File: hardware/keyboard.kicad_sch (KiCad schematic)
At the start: 41 parts, among them SW1 SW_Push, SW10 SW_Push, SW11 SW_Push, SW12 SW_Push, SW13 SW_Push, SW14 SW_Push, SW15 SW_Push, SW16 SW_Push, SW17 SW_Push, SW18 SW_Push, SW19 SW_Push, SW2 SW_Push, SW20 SW_Push, SW21 SW_Push, SW22 SW_Push, SW23 SW_Push, SW24 SW_Push, SW25 SW_Push, SW26 SW_Push, SW27 SW_Push, SW28 SW_Push, SW29 SW_Push, SW3 SW_Push, SW30 SW_Push, SW31 SW_Push, SW32 SW_Push, SW33 SW_Push, SW34 SW_Push, SW35 SW_Push, SW36 SW_Push, SW37 SW_Push, SW38 SW_Push, SW39 SW_Push, SW4 SW_Push, SW40 SW_Push, SW5 SW_Push, SW6 SW_Push, SW7 SW_Push, SW8 SW_Push, SW9 SW_Push, U2 74HC138

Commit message: keyboard schematic
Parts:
- added R23, R24, R25, R26, R27, R28, R29, R30: 22, symbol Device:R
- added SW42, SW43, SW44, SW45, SW46, SW47, SW48, SW49, SW50, SW51, SW52, SW53, SW54, SW55, SW56, SW57: SW_Push, Button_Switch_SMD:SW_Push_1P1T_NO_6x6mm_H9.5mm, symbol Switch:SW_Push
- U2: LCSC (none) -> C2906780
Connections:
- net at SW34.1: now also SW28.1, SW29.1, SW30.1, SW31.1, SW32.1, SW35.1, R26.2
- net KB_COL5: now reaches SW34.2
- net KB_COL5: now also SW10.2, SW18.2, SW26.2, SW3.2, SW42.2, SW49.2, SW56.2
- net at SW14.1: now also SW12.1, SW13.1, SW15.1, SW16.1, SW18.1, SW19.1, R28.2
- net KB_COL2: now reaches SW14.2
- net KB_COL2: now also SW17.2, SW22.2, SW30.2, SW38.2, SW6.2, SW46.2, SW53.2
- net at SW33.1: now also SW1.1, SW17.1, SW25.1, SW3.1, SW4.1, SW9.1, R30.2
- net KB_COL4: now reaches SW33.2
- net KB_COL4: now also SW16.2, SW24.2, SW32.2, SW40.2, SW8.2, SW48.2, SW55.2
- net at SW6.1: now also SW10.1, SW11.1, SW2.1, SW5.1, SW7.1, SW8.1, R29.2
- net KB_COL3: now reaches SW31.2
- net KB_COL3: now also SW15.2, SW23.2, SW25.2, SW39.2, SW7.2, SW47.2, SW54.2
- net KB_COL1: now reaches SW9.2
- net KB_COL1: now also SW13.2, SW21.2, SW29.2, SW37.2, SW5.2, SW45.2, SW52.2
- net KB_COL6: now reaches SW11.2
- net KB_COL6: now also SW19.2, SW27.2, SW35.2, SW4.2, SW43.2, SW50.2, SW57.2
- net at SW39.1: now also SW36.1, SW37.1, SW38.1, SW40.1, R25.2, SW42.1, SW43.1
- net KB_COL0: now reaches SW1.2
- net KB_COL0: now also SW12.2, SW2.2, SW20.2, SW28.2, SW36.2, SW44.2, SW51.2
- net at SW23.1: now also SW20.1, SW21.1, SW22.1, SW24.1, SW26.1, SW27.1, R27.2
- net KB_ROW0: now reaches U2.1 (A0)
- net at U2.10 (~{Y5}): now also R28.1
- net at U2.11 (~{Y4}): now also R27.1
- net at U2.12 (~{Y3}): now also R26.1
- net at U2.13 (~{Y2}): now also R25.1
- net at U2.14 (~{Y1}): now also R24.1
- net at U2.15 (~{Y0}): now also R23.1
- net +3.3V: now reaches U2.16 (VCC)
- net +3.3V: now also U2.6 (E2)
- net KB_ROW1: now reaches U2.2 (A1)
- net KB_ROW2: now reaches U2.3 (A2)
- net GND: now reaches U2.4 (~{E0})
- net GND: now also U2.5 (~{E1}), U2.8 (GND)
- net at U2.7 (~{Y7}): now also R30.1
- net at U2.9 (~{Y6}): now also R29.1
- new net: R24.2, SW44.1, SW45.1, SW46.1, SW47.1, SW48.1, SW49.1, SW50.1
- new net: R23.2, SW51.1, SW52.1, SW53.1, SW54.1, SW55.1, SW56.1, SW57.1
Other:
- moved on the sheet: SW1, SW17, SW25, SW33, SW9, U2

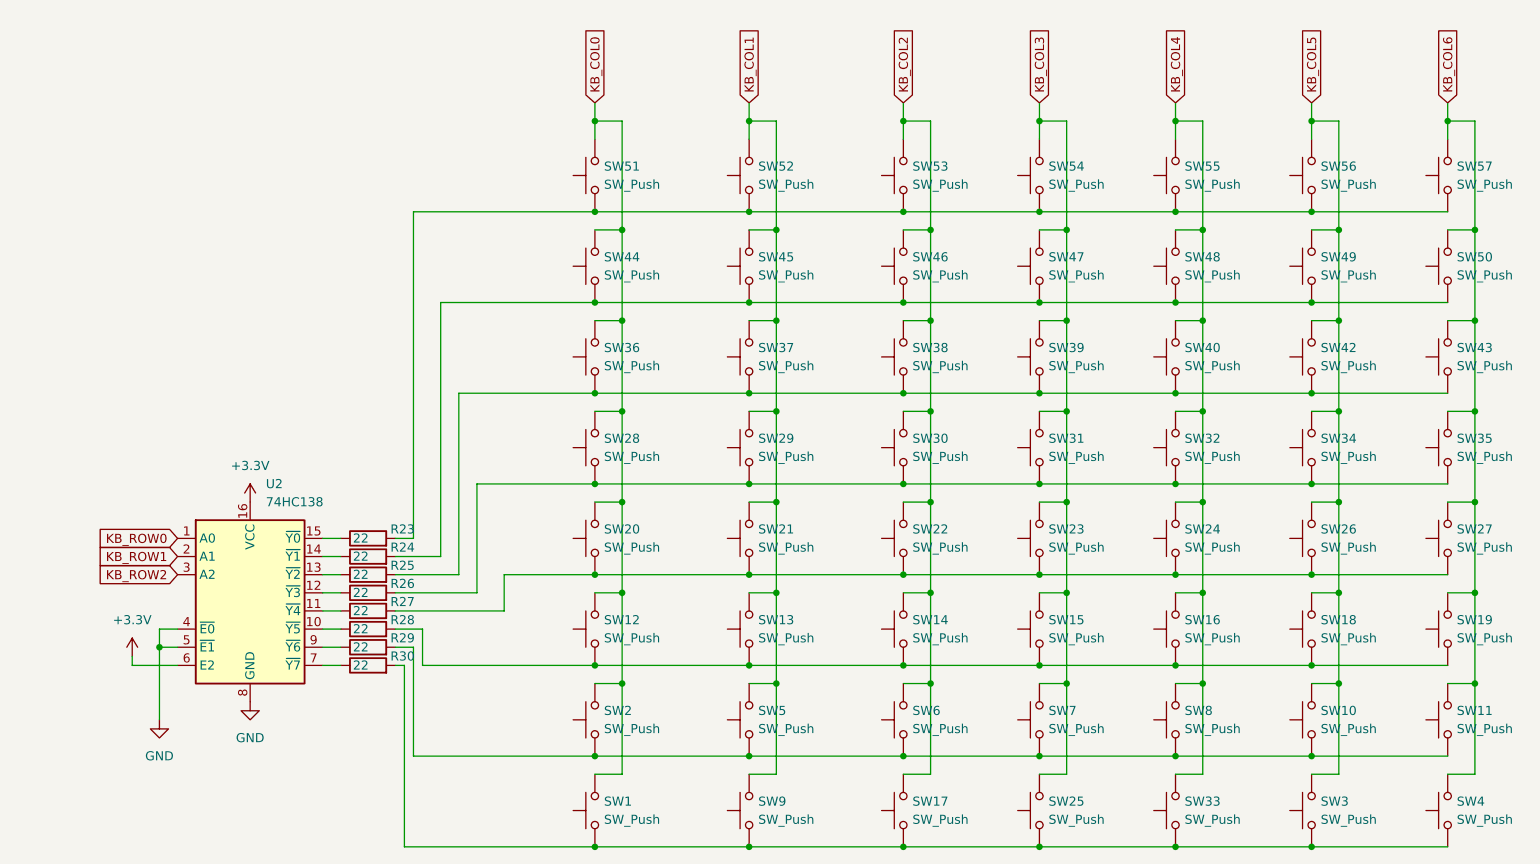
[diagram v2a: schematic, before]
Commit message: update usb port, esd, lcsc
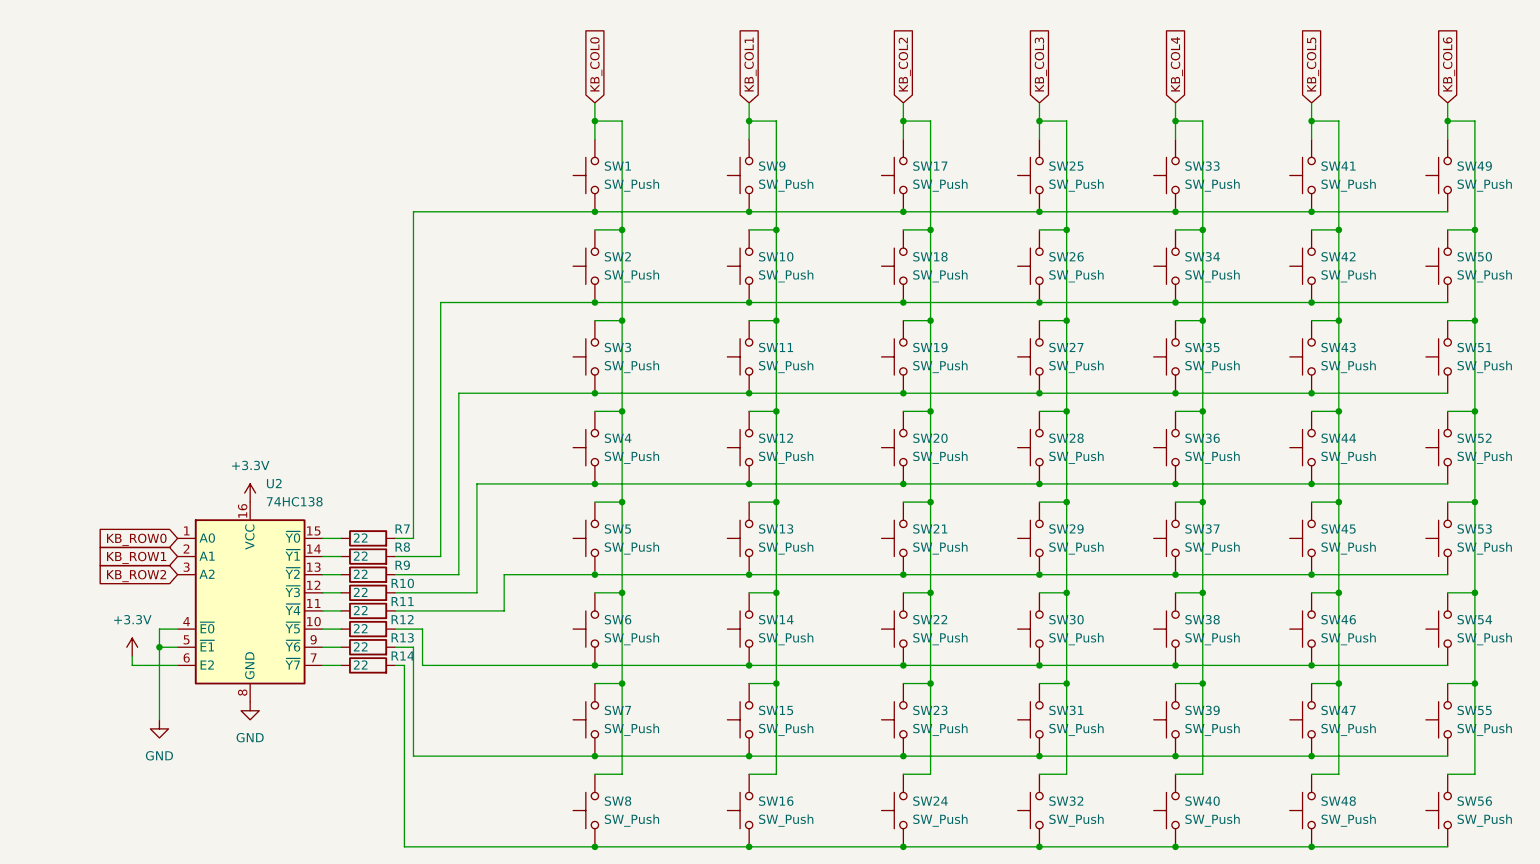
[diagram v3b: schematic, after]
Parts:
- renumbered R26 to R10, R27 to R11, R28 to R12, R29 to R13, R30 to R14, R23 to R7, R24 to R8, R25 to R9, SW51 to SW1, SW45 to SW10, SW37 to SW11, SW29 to SW12, SW21 to SW13, SW13 to SW14, SW5 to SW15, SW9 to SW16, SW53 to SW17, SW46 to SW18, SW38 to SW19, SW44 to SW2, SW30 to SW20, SW22 to SW21, SW14 to SW22, SW6 to SW23, SW17 to SW24, SW54 to SW25, SW47 to SW26, SW39 to SW27, SW31 to SW28, SW23 to SW29, SW36 to SW3, SW15 to SW30, SW7 to SW31, SW25 to SW32, SW55 to SW33, SW48 to SW34, SW40 to SW35, SW32 to SW36, SW24 to SW37, SW16 to SW38, SW8 to SW39, SW28 to SW4, SW33 to SW40, SW56 to SW41, SW49 to SW42, SW42 to SW43, SW34 to SW44, SW26 to SW45, SW18 to SW46, SW10 to SW47, SW3 to SW48, SW57 to SW49, SW20 to SW5, SW43 to SW51, SW35 to SW52, SW27 to SW53, SW19 to SW54, SW11 to SW55, SW4 to SW56, SW12 to SW6, SW2 to SW7, SW1 to SW8, SW52 to SW9

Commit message: remove global labels
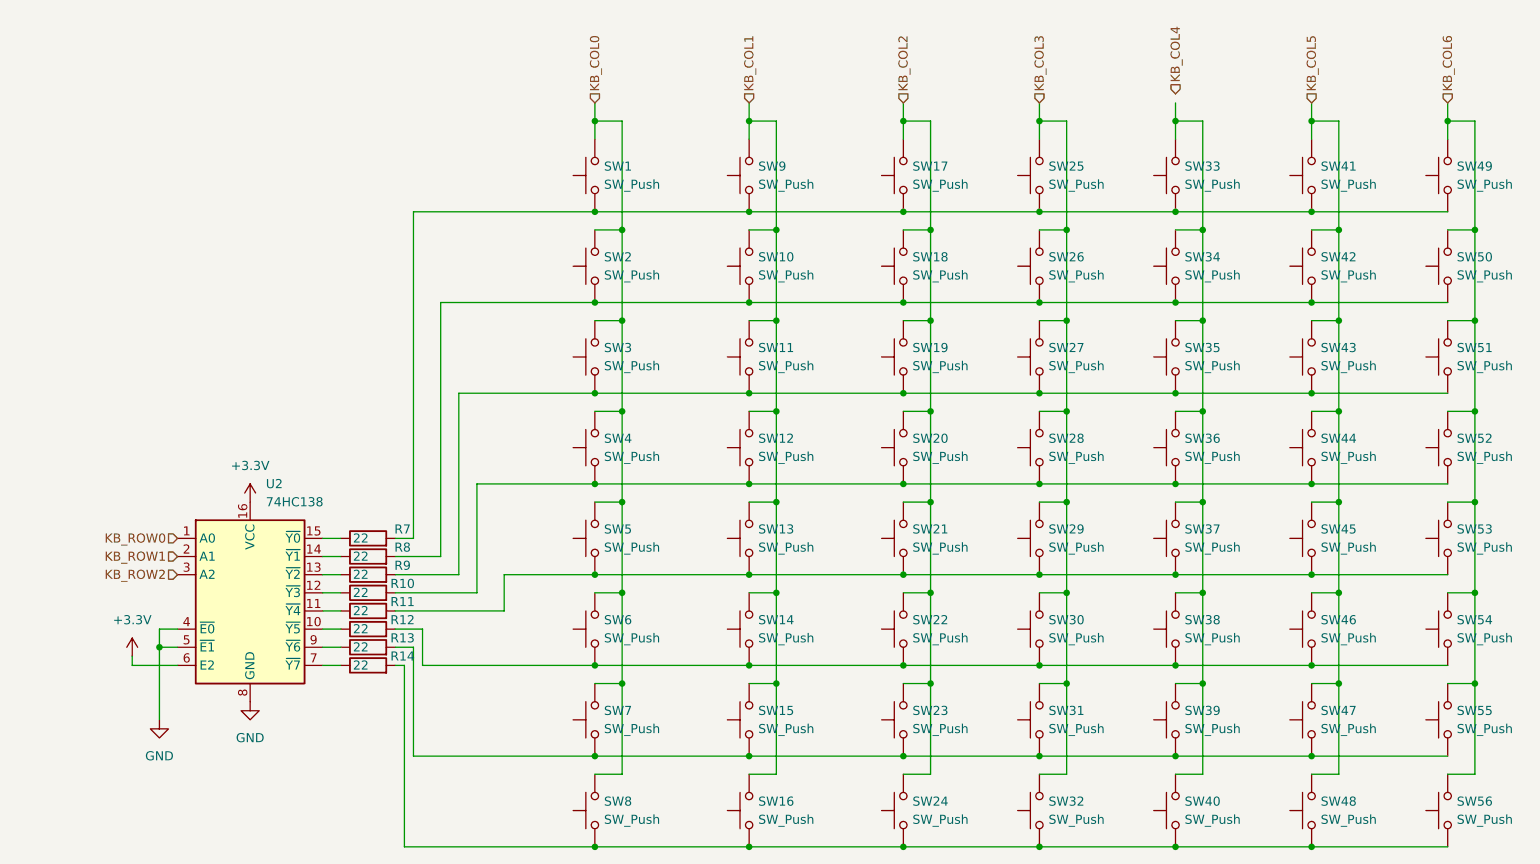
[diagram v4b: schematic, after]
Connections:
- net KB_COL4: no longer SW33.2, SW34.2, SW35.2, SW36.2, SW37.2, SW38.2, SW39.2, SW40.2
- new net: SW33.2, SW34.2, SW35.2, SW36.2, SW37.2, SW38.2, SW39.2, SW40.2
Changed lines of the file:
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@@
 		)
 	)
-	(global_label "KB_ROW2"
+	(hierarchical_label "KB_ROW0"
+		(shape input)
+		(at 57.15 109.22 180)
+		(fields_autoplaced yes)
+		(effects
+			(font
+				(size 1.27 1.27)
+			)
+			(justify right)
+		)
+	)
+	(hierarchical_label "KB_COL3"
+		(shape input)
+		(at 177.8 48.26 90)
+		(fields_autoplaced yes)
+		(effects
+			(font
+				(size 1.27 1.27)
+			)
+			(justify left)
+		)
+	)
+	(hierarchical_label "KB_COL2"
+		(shape input)
+		(at 158.75 48.26 90)
+		(fields_autoplaced yes)
+		(effects
+			(font
+				(size 1.27 1.27)
+			)
+			(justify left)
+		)
+	)
+	(hierarchical_label "KB_ROW1"
+		(shape input)
+		(at 57.15 111.76 180)
+		(fields_autoplaced yes)
+		(effects
+			(font
+				(size 1.27 1.27)
+			)
+			(justify right)
+		)
+	)
+	(hierarchical_label "KB_COL5"
+		(shape input)
+		(at 215.9 48.26 90)
+		(fields_autoplaced yes)
+		(effects
+			(font
+				(size 1.27 1.27)
+			)
+			(justify left)
+		)
+	)
+	(hierarchical_label "KB_COL6"
+		(shape input)
+		(at 234.95 48.26 90)
+		(fields_autoplaced yes)
+		(effects
+			(font
+				(size 1.27 1.27)
+			)
+			(justify left)
+		)
+	)
+	(hierarchical_label "KB_COL1"
+		(shape input)
+		(at 137.16 48.26 90)
+		(fields_autoplaced yes)
+		(effects
+			(font
+				(size 1.27 1.27)
+			)
+			(justify left)
+		)
+	)
+	(hierarchical_label "KB_ROW2"
 		(shape input)
 		(at 57.15 114.3 180)
@@
 			(justify right)
 		)
-		(property "Intersheetrefs" "${INTERSHEET_REFS}"
-			(at 45.3958 114.3 0)
-			(effects
-				(font
-					(size 1.27 1.27)
-				)
-				(justify right)
-				(hide yes)
-			)
-		)
 	)
-	(global_label "KB_COL5"
-		(shape input)
-		(at 215.9 48.26 90)
-		(fields_autoplaced yes)
-		(effects
-			(font
-				(size 1.27 1.27)
-			)
-			(justify left)
-		)
-		(property "Intersheetrefs" "${INTERSHEET_REFS}"
-			(at 215.9 36.9291 90)
-			(effects
-				(font
-					(size 1.27 1.27)
-				)
-				(justify left)
-				(hide yes)
-			)
-		)
-	)
-	(global_label "KB_COL6"
-		(shape input)
-		(at 234.95 48.26 90)
-		(fields_autoplaced yes)
-		(effects
-			(font
-				(size 1.27 1.27)
-			)
-			(justify left)
-		)
-		(property "Intersheetrefs" "${INTERSHEET_REFS}"
-			(at 234.95 36.9291 90)
-			(effects
-				(font
-					(size 1.27 1.27)
-				)
-				(justify left)
-				(hide yes)
-			)
-		)
-	)
-	(global_label "KB_COL3"
-		(shape input)
-		(at 177.8 48.26 90)
-		(fields_autoplaced yes)
-		(effects
-			(font
-				(size 1.27 1.27)
-			)
-			(justify left)
-		)
-		(property "Intersheetrefs" "${INTERSHEET_REFS}"
-			(at 177.8 36.9291 90)
-			(effects
-				(font
-					(size 1.27 1.27)
-				)
-				(justify left)
-				(hide yes)
-			)
-		)
-	)
-	(global_label "KB_COL4"
-		(shape input)
-		(at 196.85 48.26 90)
-		(fields_autoplaced yes)
-		(effects
-			(font
-				(size 1.27 1.27)
-			)
-			(justify left)
-		)
-		(property "Intersheetrefs" "${INTERSHEET_REFS}"
-			(at 196.85 36.9291 90)
-			(effects
-				(font
-					(size 1.27 1.27)
-				)
-				(justify left)
-				(hide yes)
-			)
-		)
-	)
-	(global_label "KB_ROW1"
-		(shape input)
-		(at 57.15 111.76 180)
-		(fields_autoplaced yes)
-		(effects
-			(font
-				(size 1.27 1.27)
-			)
-			(justify right)
-		)
-		(property "Intersheetrefs" "${INTERSHEET_REFS}"
-			(at 45.3958 111.76 0)
-			(effects
-				(font
-					(size 1.27 1.27)
-				)
-				(justify right)
-				(hide yes)
-			)
-		)
-	)
-	(global_label "KB_ROW0"
-		(shape input)
-		(at 57.15 109.22 180)
-		(fields_autoplaced yes)
-		(effects
-			(font
-				(size 1.27 1.27)
-			)
-			(justify right)
-		)
-		(property "Intersheetrefs" "${INTERSHEET_REFS}"
-			(at 45.3958 109.22 0)
-			(effects
-				(font
-					(size 1.27 1.27)
-				)
-				(justify right)
-				(hide yes)
-			)
-		)
-	)
-	(global_label "KB_COL1"
-		(shape input)
-		(at 137.16 48.26 90)
-		(fields_autoplaced yes)
-		(effects
-			(font
-				(size 1.27 1.27)
-			)
-			(justify left)
-		)
-		(property "Intersheetrefs" "${INTERSHEET_REFS}"
-			(at 137.16 36.9291 90)
-			(effects
-				(font
-					(size 1.27 1.27)
-				)
-				(justify left)
-				(hide yes)
-			)
-		)
-	)
-	(global_label "KB_COL2"
-		(shape input)
-		(at 158.75 48.26 90)
-		(fields_autoplaced yes)
-		(effects
-			(font
-				(size 1.27 1.27)
-			)
-			(justify left)
-		)
-		(property "Intersheetrefs" "${INTERSHEET_REFS}"
-			(at 158.75 36.9291 90)
-			(effects
-				(font
-					(size 1.27 1.27)
-				)
-				(justify left)
-				(hide yes)
-			)
-		)
-	)
-	(global_label "KB_COL0"
+	(hierarchical_label "KB_COL0"
 		(shape input)
 		(at 115.57 48.26 90)
@@
 			(justify left)
 		)
-		(property "Intersheetrefs" "${INTERSHEET_REFS}"
-			(at 115.57 36.9291 90)
-			(effects
-				(font
-					(size 1.27 1.27)
-				)
-				(justify left)
-				(hide yes)
+	)
+	(hierarchical_label "KB_COL4"
+		(shape input)
+		(at 196.85 46.99 90)
+		(fields_autoplaced yes)
+		(effects
+			(font
+				(size 1.27 1.27)
 			)
+			(justify left)
 		)
 	)

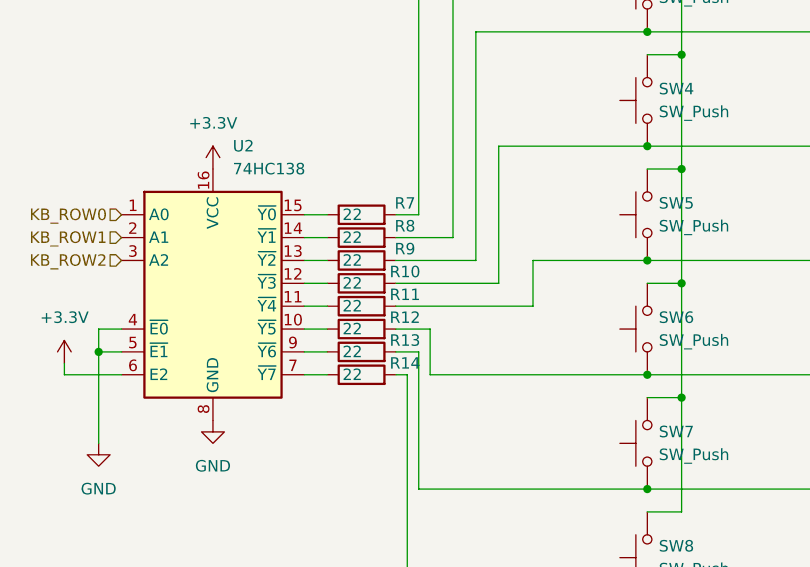
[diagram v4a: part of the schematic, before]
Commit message: add bme280
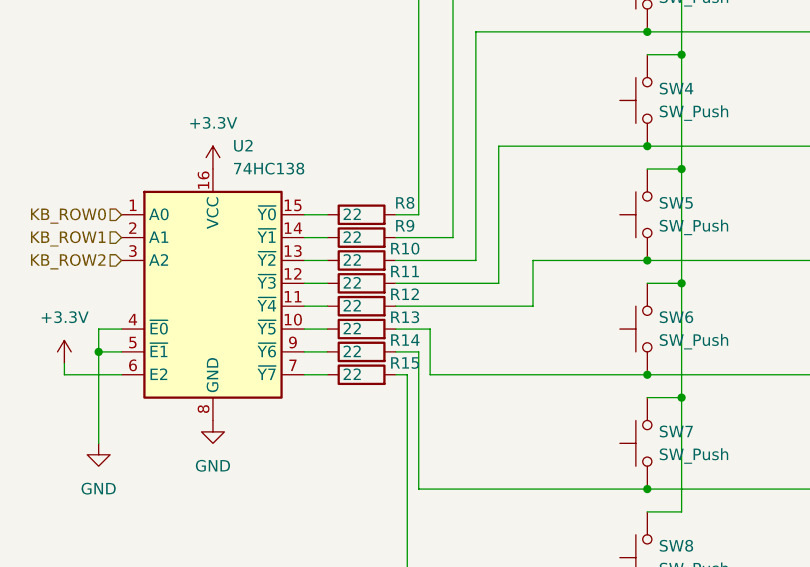
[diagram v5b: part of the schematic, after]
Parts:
- renumbered R9 to R10, R10 to R11, R11 to R12, R12 to R13, R13 to R14, R14 to R15, R7 to R8, R8 to R9
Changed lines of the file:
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@@
 		(on_board yes)
 		(dnp no)
-		(property "Reference" "R13"
+		(property "Reference" "R14"
 			(at 88.646 123.19 90)
 			(effects
@@
 			(project "badge"
 				(path "/dc4a3d77-b0f8-4e90-a4be-3e93c7025348/c21a255b-57d7-42f2-a297-078efe3a9c86"
-					(reference "R13")
+					(reference "R14")
 					(unit 1)
 				)
@@
 		(dnp no)
 		(fields_autoplaced yes)
-		(property "Reference" "#PWR08"
+		(property "Reference" "#PWR09"
 			(at 67.31 107.95 0)
 			(effects
@@
 			(project "badge"
 				(path "/dc4a3d77-b0f8-4e90-a4be-3e93c7025348/c21a255b-57d7-42f2-a297-078efe3a9c86"
-					(reference "#PWR08")
+					(reference "#PWR09")
 					(unit 1)
 				)
@@
 		(on_board yes)
 		(dnp no)
-		(property "Reference" "R8"
+		(property "Reference" "R9"
 			(at 88.646 110.49 90)
 			(effects
@@
 			(project "badge"
 				(path "/dc4a3d77-b0f8-4e90-a4be-3e93c7025348/c21a255b-57d7-42f2-a297-078efe3a9c86"
-					(reference "R8")
+					(reference "R9")
 					(unit 1)
 				)
@@
 		(on_board yes)
 		(dnp no)
-		(property "Reference" "R12"
+		(property "Reference" "R13"
 			(at 88.646 120.65 90)
 			(effects
@@
 			(project "badge"
 				(path "/dc4a3d77-b0f8-4e90-a4be-3e93c7025348/c21a255b-57d7-42f2-a297-078efe3a9c86"
-					(reference "R12")
+					(reference "R13")
 					(unit 1)
 				)
@@
 		(on_board yes)
 		(dnp no)
-		(property "Reference" "R10"
+		(property "Reference" "R11"
 			(at 88.646 115.57 90)
 			(effects
@@
 			(project "badge"
 				(path "/dc4a3d77-b0f8-4e90-a4be-3e93c7025348/c21a255b-57d7-42f2-a297-078efe3a9c86"
-					(reference "R10")
+					(reference "R11")
 					(unit 1)
 				)
@@
 		(on_board yes)
 		(dnp no)
-		(property "Reference" "R7"
+		(property "Reference" "R8"
 			(at 88.646 107.95 90)
 			(effects
@@
 			(project "badge"
 				(path "/dc4a3d77-b0f8-4e90-a4be-3e93c7025348/c21a255b-57d7-42f2-a297-078efe3a9c86"
-					(reference "R7")
+					(reference "R8")
 					(unit 1)
 				)
@@
 		(dnp no)
 		(fields_autoplaced yes)
-		(property "Reference" "#PWR07"
+		(property "Reference" "#PWR08"
 			(at 54.61 140.97 0)
 			(effects
@@
 			(project "badge"
 				(path "/dc4a3d77-b0f8-4e90-a4be-3e93c7025348/c21a255b-57d7-42f2-a297-078efe3a9c86"
-					(reference "#PWR07")
+					(reference "#PWR08")
 					(unit 1)
 				)
@@
 		(on_board yes)
 		(dnp no)
-		(property "Reference" "R11"
+		(property "Reference" "R12"
 			(at 88.646 118.11 90)
 			(effects
@@
 			(project "badge"
 				(path "/dc4a3d77-b0f8-4e90-a4be-3e93c7025348/c21a255b-57d7-42f2-a297-078efe3a9c86"
-					(reference "R11")
+					(reference "R12")
 					(unit 1)
 				)
@@
 		(dnp no)
 		(fields_autoplaced yes)
-		(property "Reference" "#PWR06"
+		(property "Reference" "#PWR07"
 			(at 50.8 129.54 0)
 			(effects
@@
 			(project "badge"
 				(path "/dc4a3d77-b0f8-4e90-a4be-3e93c7025348/c21a255b-57d7-42f2-a297-078efe3a9c86"
-					(reference "#PWR06")
+					(reference "#PWR07")
 					(unit 1)
 				)
@@
 		(on_board yes)
 		(dnp no)
-		(property "Reference" "R9"
+		(property "Reference" "R10"
 			(at 88.646 113.03 90)
 			(effects
@@
 			(project "badge"
 				(path "/dc4a3d77-b0f8-4e90-a4be-3e93c7025348/c21a255b-57d7-42f2-a297-078efe3a9c86"
-					(reference "R9")
+					(reference "R10")
 					(unit 1)
 				)
@@
 		(on_board yes)
 		(dnp no)
-		(property "Reference" "R14"
+		(property "Reference" "R15"
 			(at 88.646 125.73 90)
 			(effects
@@
 			(project "badge"
 				(path "/dc4a3d77-b0f8-4e90-a4be-3e93c7025348/c21a255b-57d7-42f2-a297-078efe3a9c86"
-					(reference "R14")
+					(reference "R15")
 					(unit 1)
 				)
@@
 		(dnp no)
 		(fields_autoplaced yes)
-		(property "Reference" "#PWR09"
+		(property "Reference" "#PWR010"
 			(at 67.31 138.43 0)
 			(effects
@@
 			(project "badge"
 				(path "/dc4a3d77-b0f8-4e90-a4be-3e93c7025348/c21a255b-57d7-42f2-a297-078efe3a9c86"
-					(reference "#PWR09")
+					(reference "#PWR010")
 					(unit 1)
 				)
